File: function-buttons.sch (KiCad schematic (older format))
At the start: 55 parts

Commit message: Initial PCB routed
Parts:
- removed C?: 100nF, symbol Device:C_Small
- removed Q? (x10): 2N3904, Package_TO_SOT_THT:TO-92_Inline, symbol Transistor_BJT:2N3904
- removed RN?: R_Network10, Resistor_THT:R_Array_SIP11, symbol Device:R_Network10
- removed U? (x7): 74HC14, symbol 74xx:74HC14
- added Q1, Q10, Q2, Q3, Q4, Q5, Q6, Q7, Q8, Q9: MMBT3904, Package_TO_SOT_SMD:SOT-23, symbol Transistor_BJT:MMBT3904
- added R54, R55, R56, R57, R58, R59, R60, R61, R62, R63, R74, R75, R76, R77, R78, R79, R80, R81, R82, R83: 1K, Resistor_SMD:R_0603_1608Metric_Pad0.98x0.95mm_HandSolder, symbol Device:R_Small
- added U14, U15: 74LVC2G14, Package_TO_SOT_SMD:SOT-23-6_Handsoldering, symbol 74xGxx:74LVC2G14
- added unit 5 of U2
- added unit 6 of U2
- C1, C10, C11, C12, C2, C3, C4, C5, C6, C7, C9: renamed from C?; footprint (none) -> Capacitor_SMD:C_0603_1608Metric_Pad1.08x0.95mm_HandSolder
- R1, R10, R2, R3, R4, R5, R6, R7, R8, R9: renamed from R?; footprint (none) -> Resistor_SMD:R_0603_1608Metric_Pad0.98x0.95mm_HandSolder
- SW1, SW10, SW2, SW3, SW4, SW5, SW6, SW7, SW8, SW9: renamed from SW?; footprint (none) -> TL-1240:TL-1240
- U2: renamed from U?; footprint (none) -> Package_SO:SSOP-14_5.3x6.2mm_P0.65mm
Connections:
- net labels removed: a, b, c, d, e, f, g, h, i, j
- wire segments 124 -> 102
- no-connect marks 20 -> 0
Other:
- moved on the sheet: U2B, U2C

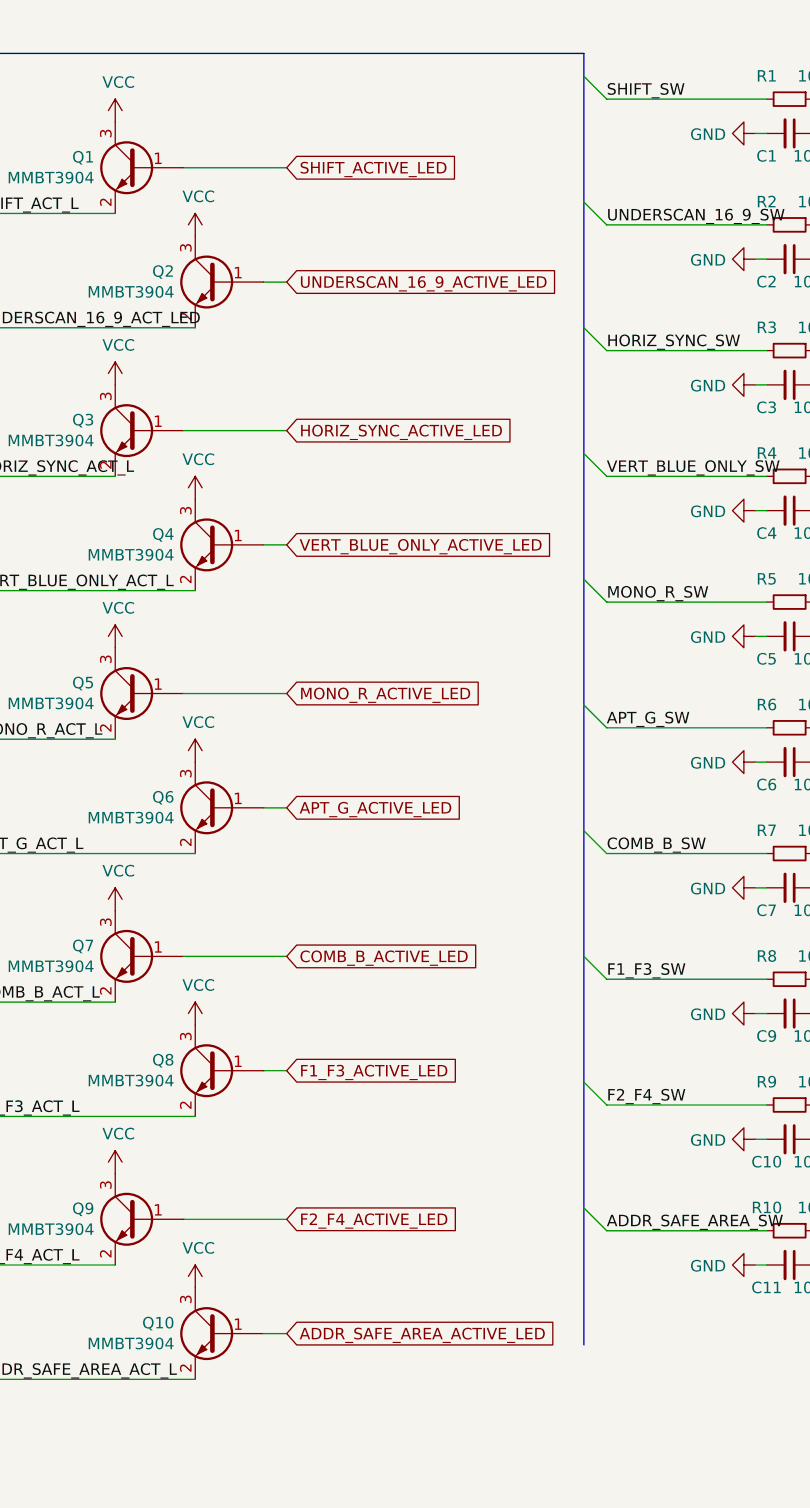
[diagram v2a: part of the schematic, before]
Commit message: A bunch of changes, full duplex 422
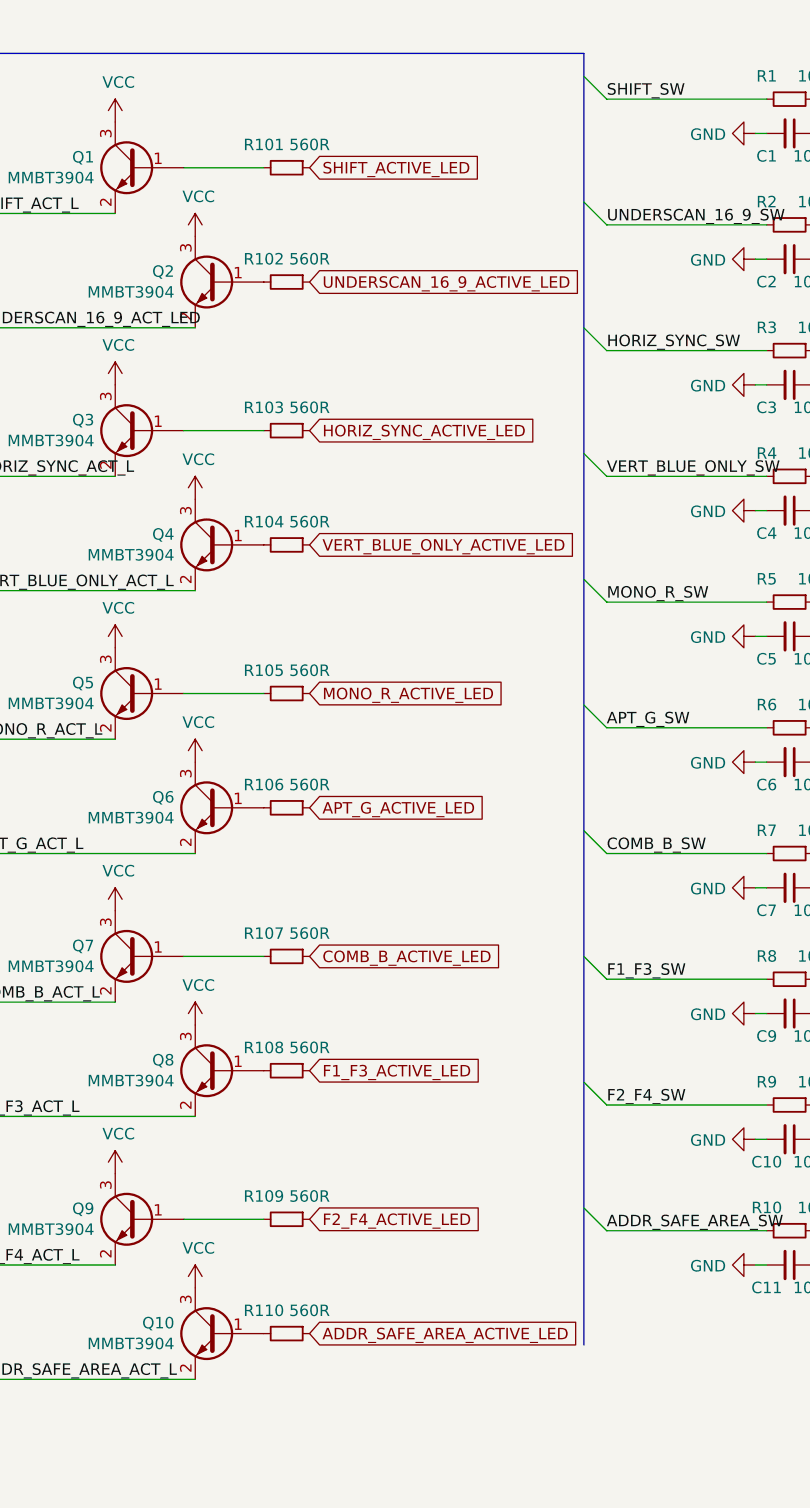
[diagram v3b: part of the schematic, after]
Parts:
- added R101, R102, R103, R104, R105, R106, R107, R108, R109, R110: 560R, Resistor_SMD:R_0603_1608Metric_Pad0.98x0.95mm_HandSolder, symbol Device:R_Small
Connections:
- net ADDR_SAFE_AREA_ACTIVE_LED: now also R110.1; no longer Q10.1 (B)
- net APT_G_ACTIVE_LED: now also R106.1; no longer Q6.1 (B)
- net COMB_B_ACTIVE_LED: now also R107.1; no longer Q7.1 (B)
- net F1_F3_ACTIVE_LED: now also R108.1; no longer Q8.1 (B)
- net F2_F4_ACTIVE_LED: now also R109.1; no longer Q9.1 (B)
- net HORIZ_SYNC_ACTIVE_LED: now also R103.1; no longer Q3.1 (B)
- net MONO_R_ACTIVE_LED: now also R105.1; no longer Q5.1 (B)
- net SHIFT_ACTIVE_LED: now also R101.1; no longer Q1.1 (B)
- net UNDERSCAN_16_9_ACTIVE_LED: now also R102.1; no longer Q2.1 (B)
- net VERT_BLUE_ONLY_ACTIVE_LED: now also R104.1; no longer Q4.1 (B)
- new net: Q2.1 (B), R102.2
- new net: Q1.1 (B), R101.2
- new net: Q3.1 (B), R103.2
- new net: Q4.1 (B), R104.2
- new net: Q5.1 (B), R105.2
- new net: Q6.1 (B), R106.2
- new net: Q7.1 (B), R107.2
- new net: Q8.1 (B), R108.2
- new net: Q9.1 (B), R109.2
- new net: Q10.1 (B), R110.2
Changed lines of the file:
@@
 Text Label 5850 1300 0    50   ~ 0
 SHIFT_ACT_L
-Text GLabel 7200 1100 2    50   Input ~ 0
+Text GLabel 7300 1100 2    50   Input ~ 0
 SHIFT_ACTIVE_LED
-Text GLabel 7200 2250 2    50   Input ~ 0
+Text GLabel 7300 2250 2    50   Input ~ 0
 HORIZ_SYNC_ACTIVE_LED
-Text GLabel 7200 1600 2    50   Input ~ 0
+Text GLabel 7300 1600 2    50   Input ~ 0
 UNDERSCAN_16_9_ACTIVE_LED
-Text GLabel 7200 2750 2    50   Input ~ 0
+Text GLabel 7300 2750 2    50   Input ~ 0
 VERT_BLUE_ONLY_ACTIVE_LED
-Text GLabel 7200 3400 2    50   Input ~ 0
+Text GLabel 7300 3400 2    50   Input ~ 0
 MONO_R_ACTIVE_LED
-Text GLabel 7200 3900 2    50   Input ~ 0
+Text GLabel 7300 3900 2    50   Input ~ 0
 APT_G_ACTIVE_LED
-Text GLabel 7200 4550 2    50   Input ~ 0
+Text GLabel 7300 4550 2    50   Input ~ 0
 COMB_B_ACTIVE_LED
-Text GLabel 7200 5050 2    50   Input ~ 0
+Text GLabel 7300 5050 2    50   Input ~ 0
 F1_F3_ACTIVE_LED
-Text GLabel 7200 5700 2    50   Input ~ 0
+Text GLabel 7300 5700 2    50   Input ~ 0
 F2_F4_ACTIVE_LED
-Text GLabel 7200 6200 2    50   Input ~ 0
+Text GLabel 7300 6200 2    50   Input ~ 0
 ADDR_SAFE_AREA_ACTIVE_LED
-Wire Wire Line
-	7100 6200 7200 6200
-Wire Wire Line
-	6750 5700 7200 5700
-Wire Wire Line
-	7100 5050 7200 5050
-Wire Wire Line
-	6750 4550 7200 4550
-Wire Wire Line
-	7100 3900 7200 3900
-Wire Wire Line
-	6750 3400 7200 3400
-Wire Wire Line
-	7100 2750 7200 2750
-Wire Wire Line
-	6750 2250 7200 2250
-Wire Wire Line
-	7100 1600 7200 1600
-Wire Wire Line
-	6750 1100 7200 1100
 Wire Bus Line
 	3150 600  5400 600
@@
 	0    -1   -1   0
 $EndComp
+$Comp
+L Device:R_Small R104
+U 1 1 618B5DAA
+P 7200 2750
+F 0 "R104" V 7100 2650 50  0000 C CNN
+F 1 "560R" V 7100 2850 50  0000 C CNN
+F 2 "Resistor_SMD:R_0603_1608Metric_Pad0.98x0.95mm_HandSolder" H 7200 2750 50  0001 C CNN
+F 3 "~" H 7200 2750 50  0001 C CNN
+	1    7200 2750
+	0    1    1    0
+$EndComp
+$Comp
+L Device:R_Small R103
+U 1 1 618C0D1C
+P 7200 2250
+F 0 "R103" V 7100 2150 50  0000 C CNN
+F 1 "560R" V 7100 2350 50  0000 C CNN
+F 2 "Resistor_SMD:R_0603_1608Metric_Pad0.98x0.95mm_HandSolder" H 7200 2250 50  0001 C CNN
+F 3 "~" H 7200 2250 50  0001 C CNN
+	1    7200 2250
+	0    1    1    0
+$EndComp
+$Comp
+L Device:R_Small R101
+U 1 1 618DA142
+P 7200 1100
+F 0 "R101" V 7100 1000 50  0000 C CNN
+F 1 "560R" V 7100 1200 50  0000 C CNN
+F 2 "Resistor_SMD:R_0603_1608Metric_Pad0.98x0.95mm_HandSolder" H 7200 1100 50  0001 C CNN
+F 3 "~" H 7200 1100 50  0001 C CNN
+	1    7200 1100
+	0    1    1    0
+$EndComp
+Wire Wire Line
+	6750 1100 7100 1100
+Wire Wire Line
+	6750 2250 7100 2250
+$Comp
+L Device:R_Small R105
+U 1 1 618EEDA0
+P 7200 3400
+F 0 "R105" V 7100 3300 50  0000 C CNN
+F 1 "560R" V 7100 3500 50  0000 C CNN
+F 2 "Resistor_SMD:R_0603_1608Metric_Pad0.98x0.95mm_HandSolder" H 7200 3400 50  0001 C CNN
+F 3 "~" H 7200 3400 50  0001 C CNN
+	1    7200 3400
+	0    1    1    0
+$EndComp
+$Comp
+L Device:R_Small R106
+U 1 1 619094EB
+P 7200 3900
+F 0 "R106" V 7100 3800 50  0000 C CNN
+F 1 "560R" V 7100 4000 50  0000 C CNN
+F 2 "Resistor_SMD:R_0603_1608Metric_Pad0.98x0.95mm_HandSolder" H 7200 3900 50  0001 C CNN
+F 3 "~" H 7200 3900 50  0001 C CNN
+	1    7200 3900
+	0    1    1    0
+$EndComp
+$Comp
+L Device:R_Small R107
+U 1 1 6190C698
+P 7200 4550
+F 0 "R107" V 7100 4450 50  0000 C CNN
+F 1 "560R" V 7100 4650 50  0000 C CNN
+F 2 "Resistor_SMD:R_0603_1608Metric_Pad0.98x0.95mm_HandSolder" H 7200 4550 50  0001 C CNN
+F 3 "~" H 7200 4550 50  0001 C CNN
+	1    7200 4550
+	0    1    1    0
+$EndComp
+$Comp
+L Device:R_Small R108
+U 1 1 6190F8E5
+P 7200 5050
+F 0 "R108" V 7100 4950 50  0000 C CNN
+F 1 "560R" V 7100 5150 50  0000 C CNN
+F 2 "Resistor_SMD:R_0603_1608Metric_Pad0.98x0.95mm_HandSolder" H 7200 5050 50  0001 C CNN
+F 3 "~" H 7200 5050 50  0001 C CNN
+	1    7200 5050
+	0    1    1    0
+$EndComp
+$Comp
+L Device:R_Small R109
+U 1 1 61913191
+P 7200 5700
+F 0 "R109" V 7100 5600 50  0000 C CNN
+F 1 "560R" V 7100 5800 50  0000 C CNN
+F 2 "Resistor_SMD:R_0603_1608Metric_Pad0.98x0.95mm_HandSolder" H 7200 5700 50  0001 C CNN
+F 3 "~" H 7200 5700 50  0001 C CNN
+	1    7200 5700
+	0    1    1    0
+$EndComp
+$Comp
+L Device:R_Small R110
+U 1 1 6191380E
+P 7200 6200
+F 0 "R110" V 7100 6100 50  0000 C CNN
+F 1 "560R" V 7100 6300 50  0000 C CNN
+F 2 "Resistor_SMD:R_0603_1608Metric_Pad0.98x0.95mm_HandSolder" H 7200 6200 50  0001 C CNN
+F 3 "~" H 7200 6200 50  0001 C CNN
+	1    7200 6200
+	0    1    1    0
+$EndComp
+Wire Wire Line
+	6750 3400 7100 3400
+Wire Wire Line
+	6750 4550 7100 4550
+Wire Wire Line
+	6750 5700 7100 5700
 Wire Bus Line
 	3450 850  3450 7150
@@
 Wire Bus Line
 	5750 850  5750 7150
+$Comp
+L Device:R_Small R102
+U 1 1 618D8BE0
+P 7200 1600
+F 0 "R102" V 7100 1500 50  0000 C CNN
+F 1 "560R" V 7100 1700 50  0000 C CNN
+F 2 "Resistor_SMD:R_0603_1608Metric_Pad0.98x0.95mm_HandSolder" H 7200 1600 50  0001 C CNN
+F 3 "~" H 7200 1600 50  0001 C CNN
+	1    7200 1600
+	0    1    1    0
+$EndComp
 $EndSCHEMATC

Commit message: Initial revision B
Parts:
- removed Q10, Q2, Q3, Q4, Q5, Q6, Q7, Q8, Q9: MMBT3904, Package_TO_SOT_SMD:SOT-23, symbol Transistor_BJT:MMBT3904
- removed R102, R103, R104, R105, R106, R107, R108, R109, R110: 560R, Resistor_SMD:R_0603_1608Metric_Pad0.98x0.95mm_HandSolder, symbol Device:R_Small
- added U201, U202, U203, U204, U205, U206, U207, U208, U209: 74LVC2G34, Package_TO_SOT_SMD:SOT-23-6_Handsoldering, symbol 74xGxx:74LVC2G34
- SW1, SW10, SW2, SW3, SW4, SW5, SW6, SW7, SW8, SW9: footprint TL-1240:TL-1240 -> TL-1265:TL-1265
- U2: footprint Package_SO:SSOP-14_5.3x6.2mm_P0.65mm -> Package_SO:TSSOP-14_4.4x5mm_P0.65mm
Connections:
- net ADDR_SAFE_AREA_ACTIVE_LED: now also U209.3
- net ADDR_SAFE_AREA_ACT_L: now also U209.4
- net APT_G_ACTIVE_LED: now also U205.3
- net APT_G_ACT_L: now also U205.4
- net COMB_B_ACTIVE_LED: now also U206.3
- net COMB_B_ACT_L: now also U206.4
- net F1_F3_ACTIVE_LED: now also U207.3
- net F1_F3_ACT_L: now also U207.4
- net F2_F4_ACTIVE_LED: now also U208.3
- net F2_F4_ACT_L: now also U208.4
- net GND: now also U201.2 (GND), U201.2 (GND), U202.2 (GND), U202.2 (GND), U203.2 (GND), U203.2 (GND), U204.2 (GND), U204.2 (GND), U205.2 (GND), U205.2 (GND), U206.2 (GND), U206.2 (GND), U207.2 (GND), U207.2 (GND), U208.2 (GND), U208.2 (GND), U209.2 (GND), U209.2 (GND); no longer R55.2, R56.2, R57.2, R58.2, R59.2, R60.2, R61.2, R62.2, R63.2
- net HORIZ_SYNC_ACTIVE_LED: now also U202.3
- net HORIZ_SYNC_ACT_L: now also U202.4
- net MONO_R_ACTIVE_LED: now also U204.3
- net MONO_R_ACT_L: now also U204.4
- net SHIFT_ACTIVE_LED: now also U201.1, U202.1, U203.1, U204.1, U205.1, U206.1, U207.1, U208.1, U209.1
- net UNDERSCAN_16_9_ACTIVE_LED: now also U201.3
- net UNDERSCAN_16_9_ACT_LED: now also U201.4
- net VCC: now also U201.5 (VCC), U201.5 (VCC), U202.5 (VCC), U202.5 (VCC), U203.5 (VCC), U203.5 (VCC), U204.5 (VCC), U204.5 (VCC), U205.5 (VCC), U205.5 (VCC), U206.5 (VCC), U206.5 (VCC), U207.5 (VCC), U207.5 (VCC), U208.5 (VCC), U208.5 (VCC), U209.5 (VCC), U209.5 (VCC)
- net VERT_BLUE_ONLY_ACTIVE_LED: now also U203.3
- net VERT_BLUE_ONLY_ACT_L: now also U203.4
- new net: R56.2, U201.6
- new net: R58.2, U204.6
- new net: R60.2, U206.6
- new net: R62.2, U208.6
- new net: R55.2, U202.6
- new net: R57.2, U203.6
- new net: R59.2, U205.6
- new net: R61.2, U207.6
- new net: R63.2, U209.6
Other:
- moved on the sheet: C1, C10, C11, C12, C2, C3, C4, C5, C6, C7, C9, Q1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
